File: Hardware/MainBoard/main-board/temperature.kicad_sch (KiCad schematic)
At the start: 27 parts, among them J10 4DB-P108-02, U5 OPA333AIDCKT, U6 OPA333AIDCKT, U7 DS18B20+

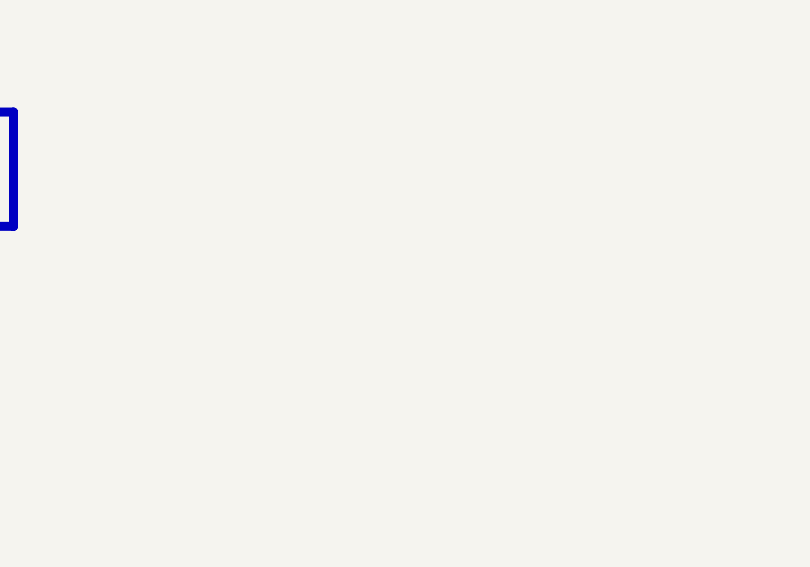
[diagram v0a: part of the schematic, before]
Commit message: add details, need to change TC amp gain for different voltage and temperature
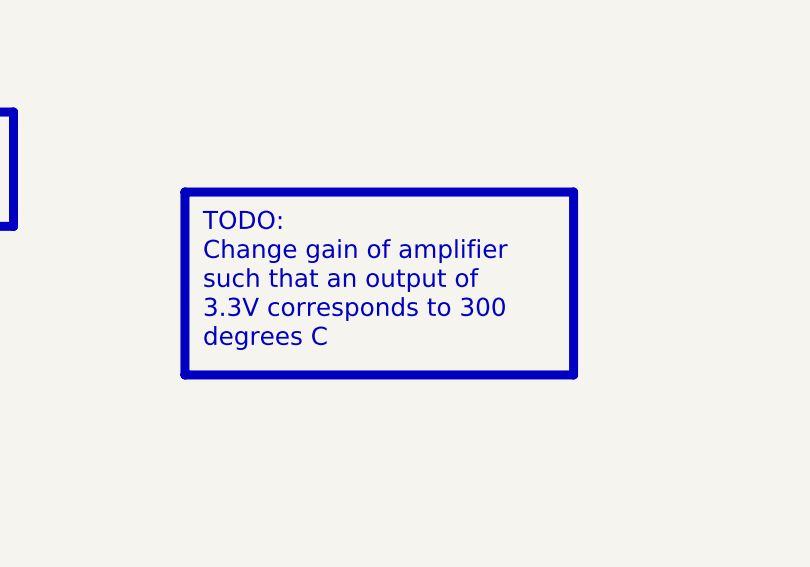
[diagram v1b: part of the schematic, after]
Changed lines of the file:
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@@
+		)
+	)
+	(text_box "TODO:\nChange gain of amplifier such that an output of 3.3V corresponds to 300 degrees C"
+		(exclude_from_sim no)
+		(at 226.06 184.15 0)
+		(size 43.18 20.32)
+		(margins 2 2 2 2)
+		(stroke
+			(width 1)
+			(type solid)
+			(color 47 219 23 1)
+		)
+		(fill
+			(type color)
+			(color 55 255 27 1)
+		)
+		(effects
+			(font
+				(face "Arial")
+				(size 2 2)
+				(color 0 0 0 1)
+			)
+			(justify left top)
 		)
 	)

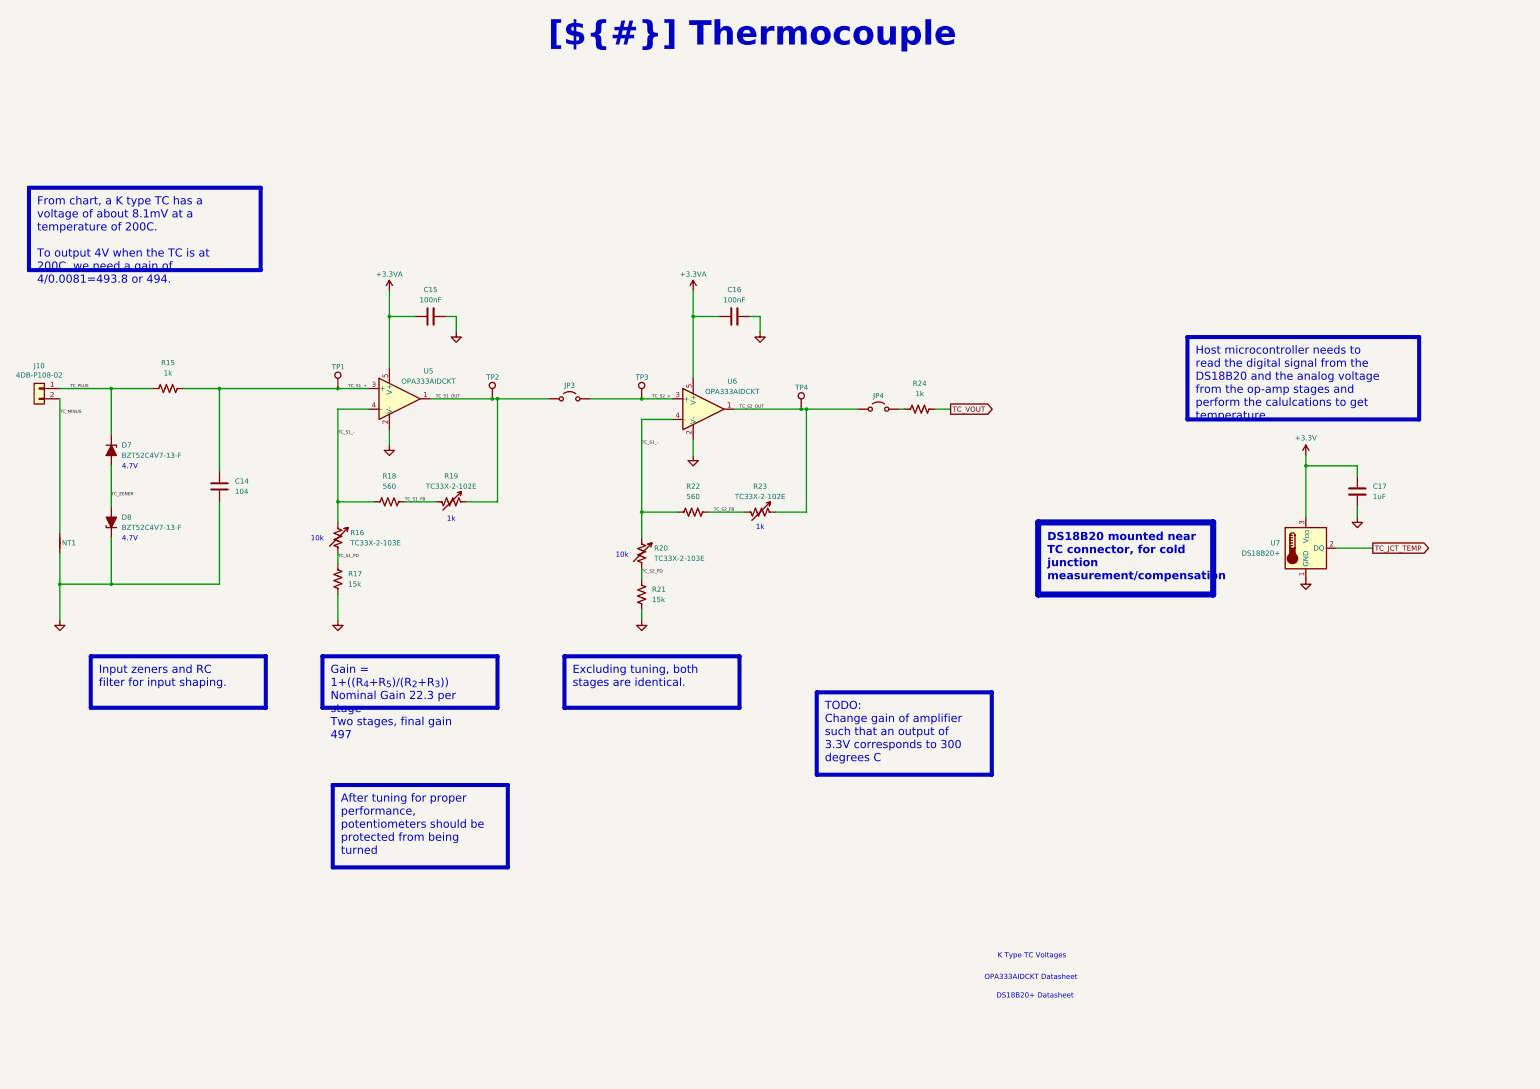
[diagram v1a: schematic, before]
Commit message: add heatsink mounting holes, change a few footprints, clean up schematic
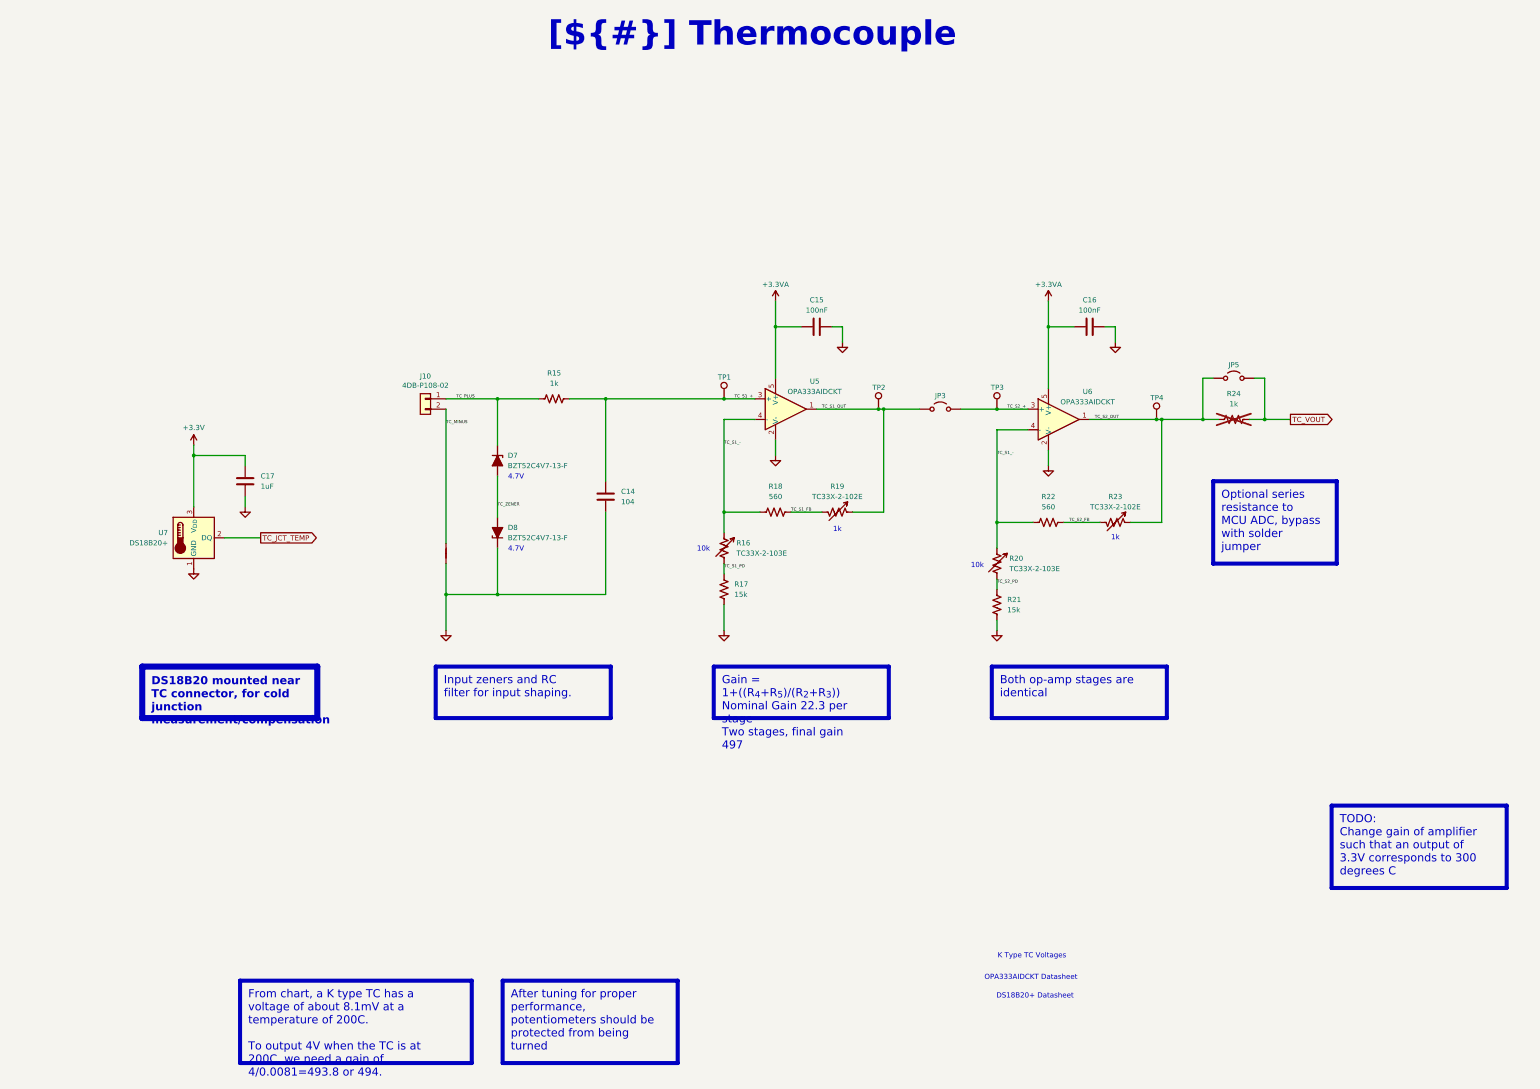
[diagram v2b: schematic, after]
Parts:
- removed JP4: Jumper_2_Open, Connector_PinHeader_2.54mm:PinHeader_1x02_P2.54mm_Vertical, symbol Jumper:Jumper_2_Open
- added JP5: Jumper_2_Open, Jumper:SolderJumper-2_P1.3mm_Open_TrianglePad1.0x1.5mm, symbol Jumper:Jumper_2_Open
- R24: now not fitted
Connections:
- net TC_S2_OUT: now also R24.1, JP5.1 (A)
- net TC_VOUT: now also JP5.2 (B)
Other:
- moved on the sheet: C14, C15, C16, C17, D7, D8, J10, JP3, R15, R16, R17, R18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

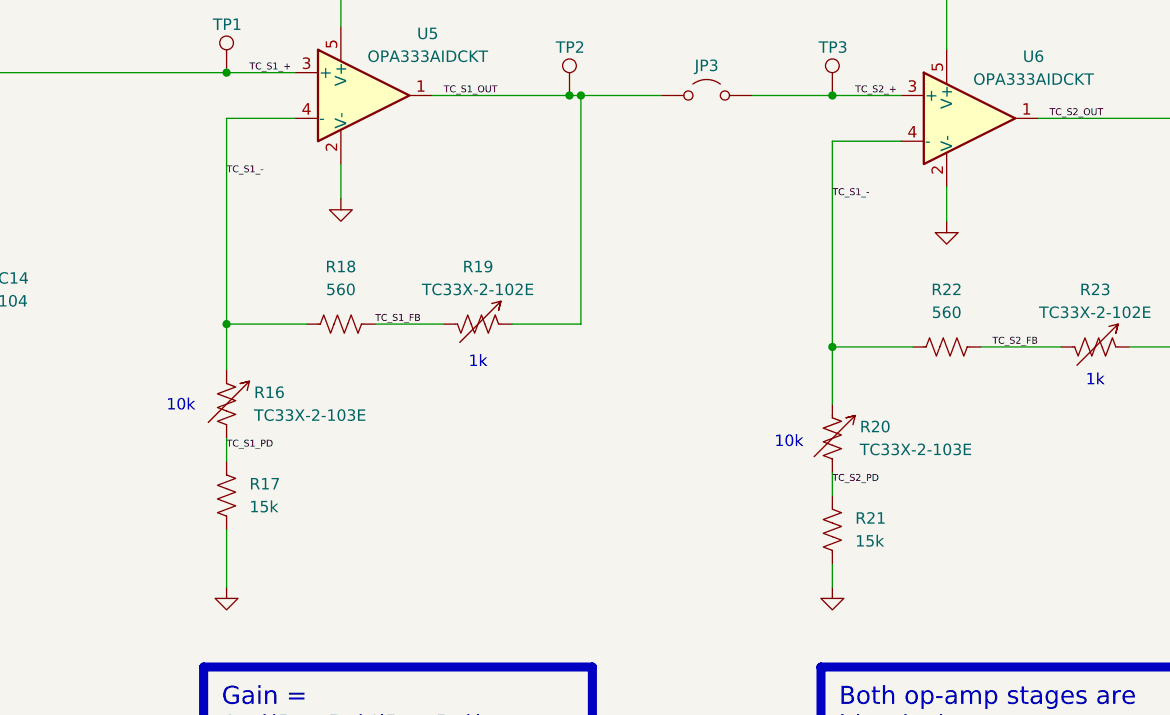
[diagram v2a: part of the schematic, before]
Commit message: routing halfway done, trying autorouter to finish low voltage signals
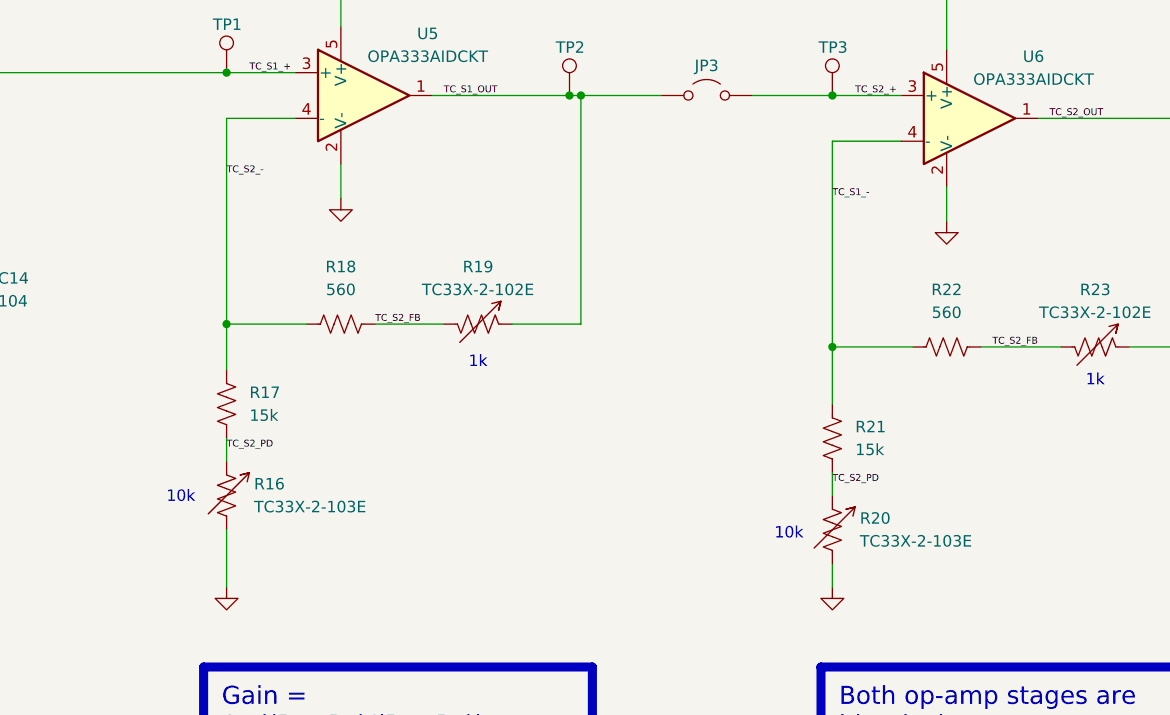
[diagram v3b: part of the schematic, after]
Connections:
- net TC_S1_FB is gone; now on net TC_S2_FB: R18.2, R19.2
- net GND: now also R16.2, R20.2; no longer R17.2, R21.2
- net TC_S1_-: now also R21.1; no longer R16.1, R18.1, R20.1, U5.4 (-)
- net TC_S2_PD: now also R16.1, R17.2, R20.1, R21.2; no longer R20.2, R21.1
- net TC_S1_PD renamed TC_S2_-
- net TC_S2_-: now also R18.1, U5.4 (-); no longer R16.2
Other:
- moved on the sheet: R16, R17, R20, R21
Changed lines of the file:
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@@
 	(text "10k"
 		(exclude_from_sim no)
-		(at 198.12 148.844 0)
+		(at 198.12 159.004 0)
 		(effects
 			(font
@@
 	(text "10k"
 		(exclude_from_sim no)
-		(at 265.684 152.908 0)
+		(at 265.684 163.068 0)
 		(effects
 			(font
@@
 		)
 	)
-	(label "TC_S1_FB"
+	(label "TC_S2_FB"
 		(at 219.71 139.7 0)
 		(effects
@@
 		)
 	)
-	(label "TC_S1_PD"
+	(label "TC_S2_PD"
 		(at 203.2 153.67 0)
 		(effects
@@
 		)
 	)
-	(label "TC_S1_-"
+	(label "TC_S2_-"
 		(at 203.2 123.19 0)
 		(effects
@@
 	(symbol
 		(lib_id "Device:R_US")
-		(at 270.51 162.56 0)
+		(at 270.51 152.4 0)
 		(unit 1)
 		(exclude_from_sim no)
@@
 		(fields_autoplaced yes)
 		(property "Reference" "R21"
-			(at 273.05 161.2899 0)
+			(at 273.05 151.1299 0)
 			(effects
 				(font
@@
 		)
 		(property "Value" "15k"
-			(at 273.05 163.8299 0)
+			(at 273.05 153.6699 0)
 			(effects
 				(font
@@
 		)
 		(property "Footprint" "Resistor_SMD:R_0603_1608Metric_Pad0.98x0.95mm_HandSolder"
-			(at 271.526 162.814 90)
+			(at 271.526 152.654 90)
 			(effects
 				(font
@@
 		)
 		(property "Datasheet" "~"
-			(at 270.51 162.56 0)
+			(at 270.51 152.4 0)
 			(effects
 				(font
@@
 		)
 		(property "Description" "Resistor, US symbol"
-			(at 270.51 162.56 0)
+			(at 270.51 152.4 0)
 			(effects
 				(font
@@
 	(symbol
 		(lib_id "Device:R_Variable_US")
-		(at 270.51 152.4 0)
+		(at 270.51 162.56 0)
 		(unit 1)
 		(exclude_from_sim no)
@@
 		(dnp no)
 		(property "Reference" "R20"
-			(at 273.558 151.13 0)
+			(at 273.558 161.29 0)
 			(effects
 				(font
@@
 		)
 		(property "Value" "TC33X-2-103E"
-			(at 273.558 153.67 0)
+			(at 273.558 163.83 0)
 			(effects
 				(font
@@
 		)
 		(property "Footprint" "Potentiometer_SMD:Potentiometer_Bourns_TC33X_Vertical"
-			(at 268.732 152.4 90)
+			(at 268.732 162.56 90)
 			(effects
 				(font
@@
 		)
 		(property "Datasheet" "~"
-			(at 270.51 152.4 0)
+			(at 270.51 162.56 0)
 			(effects
 				(font
@@
 		)
 		(property "Description" "Variable resistor, US symbol"
-			(at 270.51 152.4 0)
+			(at 270.51 162.56 0)
 			(effects
 				(font
@@
 	(symbol
 		(lib_id "Device:R_US")
-		(at 203.2 158.75 0)
+		(at 203.2 148.59 0)
 		(unit 1)
 		(exclude_from_sim no)
@@
 		(fields_autoplaced yes)
 		(property "Reference" "R17"
-			(at 205.74 157.4799 0)
+			(at 205.74 147.3199 0)
 			(effects
 				(font
@@
 		)
 		(property "Value" "15k"
-			(at 205.74 160.0199 0)
+			(at 205.74 149.8599 0)
 			(effects
 				(font
@@
 		)
 		(property "Footprint" "Resistor_SMD:R_0603_1608Metric_Pad0.98x0.95mm_HandSolder"
-			(at 204.216 159.004 90)
+			(at 204.216 148.844 90)
 			(effects
 				(font
@@
 		)
 		(property "Datasheet" "~"
-			(at 203.2 158.75 0)
+			(at 203.2 148.59 0)
 			(effects
 				(font
@@
 		)
 		(property "Description" "Resistor, US symbol"
-			(at 203.2 158.75 0)
+			(at 203.2 148.59 0)
 			(effects
 				(font
@@
 	(symbol
 		(lib_id "Device:R_Variable_US")
-		(at 203.2 148.59 0)
+		(at 203.2 158.75 0)
 		(unit 1)
 		(exclude_from_sim no)
@@
 		(dnp no)
 		(property "Reference" "R16"
-			(at 206.248 147.32 0)
+			(at 206.248 157.48 0)
 			(effects
 				(font
@@
 		)
 		(property "Value" "TC33X-2-103E"
-			(at 206.248 149.86 0)
+			(at 206.248 160.02 0)
 			(effects
 				(font
@@
 		)
 		(property "Footprint" "Potentiometer_SMD:Potentiometer_Bourns_TC33X_Vertical"
-			(at 201.422 148.59 90)
+			(at 201.422 158.75 90)
 			(effects
 				(font
@@
 		)
 		(property "Datasheet" "~"
-			(at 203.2 148.59 0)
+			(at 203.2 158.75 0)
 			(effects
 				(font
@@
 		)
 		(property "Description" "Variable resistor, US symbol"
-			(at 203.2 148.59 0)
+			(at 203.2 158.75 0)
 			(effects
 				(font
